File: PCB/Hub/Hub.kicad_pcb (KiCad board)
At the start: 2 copper layers, 98.8 x 85.2 mm, 31 parts, among them IC1 ESP32-DEVKITC-VE, IC2 Tranceiver_CAN, J1 Connecteur_male_Grove_Mabee, K1 DSY2Y-S-205H, Q2 2N2222, U1 BMP581, U10 Bornier_a_vis, U3 Bornier_a_vis, U4 DB301V-5.0-2P, U5 BMI088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

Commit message: hub
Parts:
- removed C3: 100nf, Capacitor_THT:C_Axial_L3.8mm_D2.6mm_P7.50mm_Horizontal
- removed U1: BMP581, projet:BMP581
- added D2: FR107, Bibliotheque_Projet:Diode FR107, F.Cu at (105.2, 50.5)
- added D3: FR107, Bibliotheque_Projet:Diode FR107, F.Cu at (108.0, 66.3)
- added Q1: 2N2222B, Bibliotheque_Projet:2N2222B, F.Cu at (114.3, 60.7)
- added R7: 1K, Resistor_THT:R_Axial_DIN0207_L6.3mm_D2.5mm_P10.16mm_Horizontal, F.Cu at (110.9, 66.0)
- added U2: BMP581, Bibliotheque_Projet:BMP581, F.Cu at (163.8, 83.0)
- D1: value 1N914 -> FR107; footprint Diode_THT:D_DO-41_SOD81_P12.70mm_Horizontal -> Bibliotheque_Projet:Diode FR107
- K1: value DSY2Y-S-205H -> Relais DSY2Y-S-205H
- R4: value 22k -> 10K
- R6: value 8.2k -> 3.3K
- moved R1 47.5 mm to (172.5, 50.5), turned to 180 degrees
- moved LS1 41.4 mm to (122.2, 113.0)
- moved D1 40.0 mm to (107.5, 104.2)
- moved Q2 39.2 mm to (105.3, 122.8), turned to 90 degrees
- moved R3 38.2 mm to (90.2, 120.2), turned to 0 degrees
- moved U8 33.1 mm to (88.8, 95.8), turned to -90 degrees
- moved R5 31.9 mm to (160.3, 50.5), turned to 180 degrees
- moved IC1 17.3 mm to (154.4, 70.1)
- moved R6 15.6 mm to (131.7, 57.0), turned to 180 degrees
- moved C4 13.2 mm to (150.4, 54.0)
- moved IC2 11.9 mm to (145.2, 52.0), turned to 0 degrees
- moved U5 11.7 mm to (149.5, 109.8)
- moved JP1 8.53 mm to (162.0, 38.0)
- moved U4 8.00 mm to (144.5, 45.0)
- moved U9 8.00 mm to (154.5, 45.0)
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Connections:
- net /12V renamed Vin
- IC1 pad 10: unconnected-(IC1-IO26-Pad10) -> Net-(IC1-IO26)
- IC1 pad 13: unconnected-(IC1-IO12-Pad13) -> Net-(IC1-IO12)
- IC1 pad 16: unconnected-(IC1-D2-Pad16) -> Net-(IC1-D2)
- IC1 pad 24: Net-(IC1-IO2) -> unconnected-(IC1-IO2-Pad24)
- IC1 pad 29: Net-(IC1-IO5) -> unconnected-(IC1-IO5-Pad29)
- IC1 pad 34: Net-(IC1-RX) -> unconnected-(IC1-RX-Pad34)
- IC1 pad 35: Net-(IC1-TX) -> unconnected-(IC1-TX-Pad35)
- IC1 pad 9: unconnected-(IC1-IO25-Pad9) -> Net-(IC1-IO25)
- IC2 pad 1: Net-(IC1-TX) -> Net-(IC1-IO25)
- IC2 pad 4: Net-(IC1-RX) -> Net-(IC1-IO34)
- K1 pad 1: Net-(IC1-IO35) -> +5V
- K1 pad 11: Net-(K1-NC_1) -> unconnected-(K1-NC_2-Pad11)
- K1 pad 16: GNDREF -> Net-(D3-A)
- K1 pad 6: Net-(K1-NC_1) -> unconnected-(K1-NC_1-Pad6)
- R2 pad 1: Net-(R2-Pad1) -> Net-(IC1-IO12)
- R2 pad 2: Net-(IC1-IO2) -> Net-(R2-Pad2)
- R4 pad 1: Net-(K1-NC_1) -> Net-(D2-A)
- R4 pad 2: Net-(IC1-IO34) -> Net-(IC1-IO35)
- R6 pad 1: Net-(IC1-IO34) -> GNDREF
- R6 pad 2: GNDREF -> Net-(IC1-IO35)
- U5 pad 6: Net-(IC1-IO5) -> Net-(IC1-IO26)
- U6 pad 2: Net-(K1-NC_1) -> Net-(D2-A)
- U7 pad 1: Net-(R2-Pad1) -> Net-(R2-Pad2)
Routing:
- net +3.3V: track 124.2 -> 0.00 mm
- net +5V: track 118.6 -> 0.00 mm
- net Net-(IC1-IO35): track 115.8 -> 0.00 mm
- net Net-(IC1-RX): track 101.9 -> 0.00 mm, vias 2 -> 0
- net Net-(IC1-TX): track 96.7 -> 0.00 mm, vias 2 -> 0
- net GNDREF: track 93.0 -> 0.00 mm, vias 2 -> 0
- net Net-(IC1-IO2): track 85.6 -> 0.00 mm
- net Net-(IC1-IO21): track 77.1 -> 0.00 mm, vias 1 -> 0
- net Net-(IC1-IO34): track 72.7 -> 0.00 mm
- net +12V: track 75.8 -> 13.8 mm
- net Net-(IC1-IO22): track 59.1 -> 0.00 mm
- net Net-(K1-NC_1): track 52.4 -> 0.00 mm
- net Net-(IC1-IO4): track 36.8 -> 0.00 mm
- net Net-(IC2-CANH): track 36.3 -> 0.00 mm
- net Net-(IC1-IO23): track 33.7 -> 0.00 mm
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
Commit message: HUB_PCB
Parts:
- moved R7 7.10 mm to (118.0, 66.6), turned to 90 degrees
- moved R6 6.89 mm to (130.8, 63.8), turned to 90 degrees
- moved C4 3.42 mm to (147.2, 55.2), turned to 180 degrees
- moved U2 1.75 mm to (165.5, 83.0)
- moved C2 0.75 mm to (135.0, 50.2)
- moved R4 0.25 mm to (111.4, 53.8)
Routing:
- net +5V: track 0.00 -> 157.8 mm
- net +3.3V: track 0.00 -> 108.8 mm
- net +12V: track 13.8 -> 89.8 mm
- net Net-(IC1-IO23): track 0.00 -> 62.9 mm
- net Net-(IC1-IO4): track 0.00 -> 55.9 mm
- net Net-(IC1-IO33): track 0.00 -> 54.6 mm
- net Net-(IC1-IO32): track 0.00 -> 41.2 mm
- net Net-(D3-A): track 0.00 -> 36.0 mm
- net Net-(IC1-IO35): track 0.00 -> 34.9 mm
- net Net-(IC1-IO25): track 0.00 -> 33.1 mm
- net Net-(IC1-IO22): track 0.00 -> 32.1 mm
- net Net-(IC2-CANH): track 0.00 -> 27.8 mm
- net Net-(IC2-CANL): track 0.00 -> 24.3 mm
- net Net-(IC1-IO18): track 0.00 -> 23.2 mm
- net Net-(IC2-S): track 0.00 -> 22.5 mm
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
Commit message: Hub_Version_Finale_PCB
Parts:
- moved U2 2.50 mm to (165.5, 85.5)
- moved R1 1.33 mm to (173.8, 50.5)
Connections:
- IC1 pad 29: unconnected-(IC1-IO5-Pad29) -> Net-(IC1-IO5)
- IC1 pad 3: unconnected-(IC1-VP-Pad3) -> Net-(IC1-VP)
- IC1 pad 4: unconnected-(IC1-VN-Pad4) -> Net-(IC1-VN)
- U2 pad 5: unconnected-(U2-INT-Pad5) -> Net-(IC1-IO21)
- U2 pad 6: Net-(IC1-IO21) -> Net-(IC1-IO5)
- U5 pad 8: unconnected-(U5-INT1-Pad8) -> Net-(IC1-VN)
- U5 pad 9: unconnected-(U5-INT3-Pad9) -> Net-(IC1-VP)
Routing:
- net Net-(IC1-VP): track 0.00 -> 116.5 mm, vias 0 -> 1
- net Net-(IC1-VN): track 0.00 -> 114.6 mm, vias 0 -> 1
- net Net-(IC1-IO26): track 0.00 -> 92.5 mm
- net Net-(IC1-IO13): track 0.00 -> 58.2 mm
- net Net-(IC1-IO27): track 0.00 -> 56.7 mm, vias 0 -> 1
- net Net-(IC1-IO14): track 0.00 -> 54.6 mm
- net Net-(IC1-IO5): track 0.00 -> 44.6 mm
- net Net-(IC1-IO23): track 62.9 -> 28.1 mm
- net Net-(IC1-IO21): track 0.00 -> 27.8 mm
- net Net-(IC1-IO22): track 32.1 -> 55.1 mm
- net +3.3V: track 108.8 -> 113.9 mm
- net +5V: track 157.8 -> 160.4 mm
- net Net-(IC1-IO33): track 54.6 -> 52.1 mm
- net Net-(IC1-IO32): track 41.2 -> 39.5 mm
- net Net-(D3-A): track 36.0 -> 37.5 mm
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
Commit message: Update Hub.kicad_pcb
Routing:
- net Net-(IC1-IO4): track 55.9 -> 56.7 mm
- net Net-(IC1-IO18): track 23.2 -> 22.4 mm

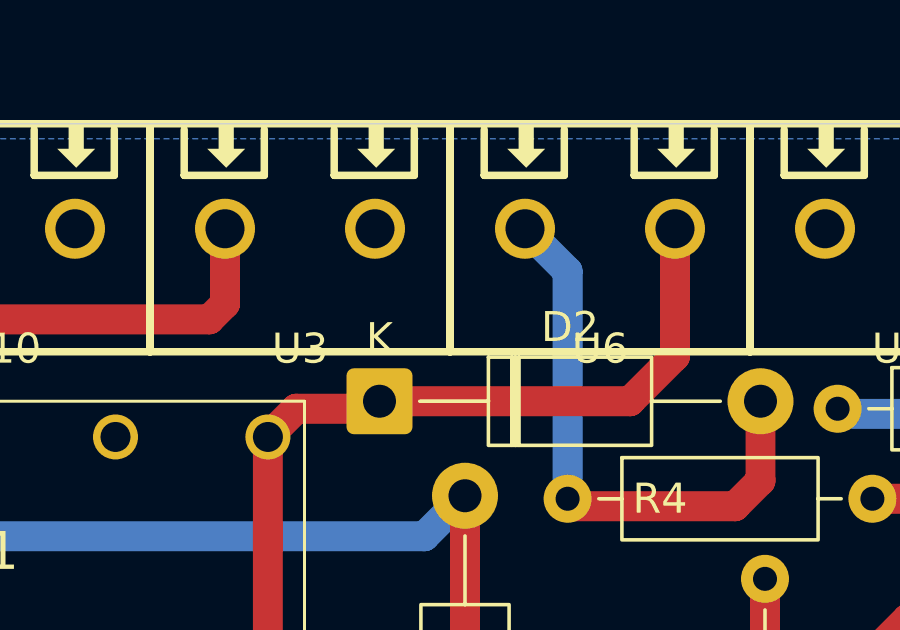
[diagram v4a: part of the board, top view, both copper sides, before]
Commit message: correction bouton PCB Kicad
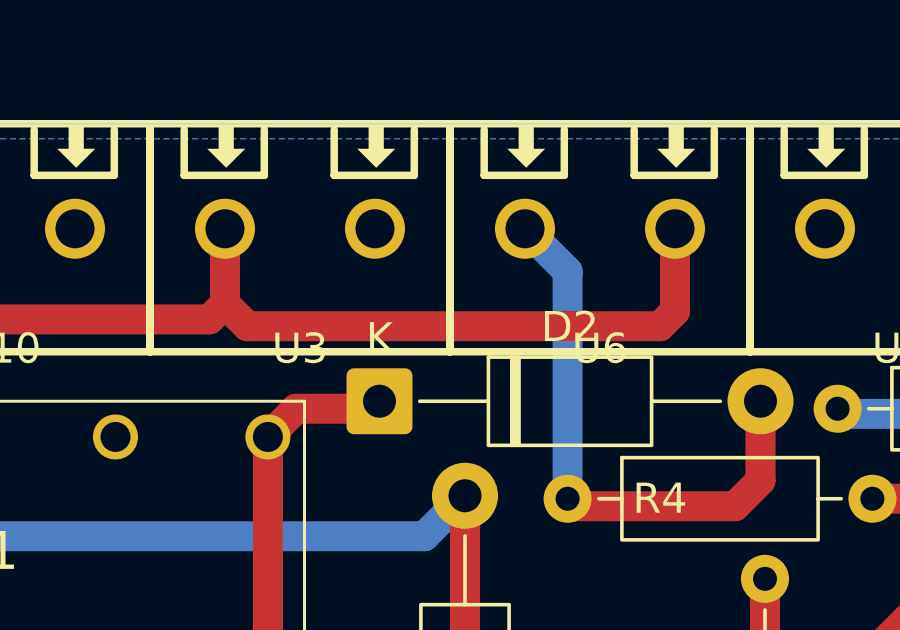
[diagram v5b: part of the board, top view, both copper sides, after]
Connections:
- U6 pad 1: +12V -> Vin
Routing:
- net Vin: track 26.5 -> 44.8 mm
- net +12V: track 89.8 -> 75.1 mm
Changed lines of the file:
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@@
 			(layers "*.Cu" "*.Mask")
 			(remove_unused_layers no)
-			(net "+12V")
+			(net "Vin")
 			(pinfunction "1_1")
 			(pintype "unspecified")
@@
 	)
 	(segment
-		(start 115 49)
-		(end 115 44.75)
-		(width 1)
-		(layer "F.Cu")
-		(net "+12V")
-	)
-	(segment
 		(start 102.37 50.75)
 		(end 104.9 50.75)
@@
 	)
 	(segment
-		(start 105.15 50.5)
-		(end 113.5 50.5)
-		(width 1)
-		(layer "F.Cu")
-		(net "+12V")
-	)
-	(segment
 		(start 119.4 104.15)
 		(end 121.25 106)
@@
 	)
 	(segment
-		(start 113.5 50.5)
-		(end 115 49)
-		(width 1)
-		(layer "F.Cu")
-		(net "+12V")
-	)
-	(segment
 		(start 103.25 64.75)
 		(end 103.25 102.25)
@@
 	)
 	(segment
+		(start 115 44.75)
+		(end 115 47.5)
+		(width 1)
+		(layer "F.Cu")
+		(net "Vin")
+	)
+	(segment
+		(start 100.75 48)
+		(end 100 47.25)
+		(width 1)
+		(layer "F.Cu")
+		(net "Vin")
+	)
+	(segment
 		(start 90 46.5)
 		(end 91.27 47.77)
@@
 	)
 	(segment
+		(start 115 47.5)
+		(end 114.5 48)
+		(width 1)
+		(layer "F.Cu")
+		(net "Vin")
+	)
+	(segment
 		(start 90 44.75)
 		(end 90 46.5)
@@
 		(width 1)
 		(layer "F.Cu")
+		(net "Vin")
+	)
+	(segment
+		(start 114.5 48)
+		(end 100.75 48)
+		(width 1)
+		(layer "F.Cu")
